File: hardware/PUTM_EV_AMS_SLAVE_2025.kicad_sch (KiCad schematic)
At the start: 7 parts, among them J1 TST-110-01-T-D, J2 M80-5100442, J4 M80-5100442

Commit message: pending
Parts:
- removed J2, J4: M80-5100442, Samacsys:M80-51004YY, symbol m80-5100442:M80-5100442
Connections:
- no-connect marks 4 -> 0

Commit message: layout done
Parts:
- removed C12, C5, C6, C9: 10nF/1kV, Capacitor_SMD:C_1206_3216Metric, symbol c2824c562jggacauto:C2824C562JGGACAUTO
- added C5, C6, C7, C8: 4.7nF/Y2, Samacsys:CAPC5728X280N, symbol Samacsys_kicad_sym:S252B222K502CT
- added J2, J3: B02B-PASK-1, Samacsys:B02BPASK1LFSN, symbol Samacsys_kicad_sym:B02B-PASK-1
- J1: footprint Connector_IDC:IDC-Header_2x09_P2.54mm_Vertical -> Connector_IDC:IDC-Header_2x10_P2.54mm_Vertical_SMD
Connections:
- net IN+: now also C7.1, J3.1 (Pin_1)
- net IN-: now also C8.1, J3.2 (Pin_2)
- net OUT+: now also C5.2, J2.1 (Pin_1)
- new net IA+: C7.2
- new net IA-: C8.2
- new net IB+: C5.1
- new net IB-: C6.1
- new net OUT-: C6.2, J2.2 (Pin_2)

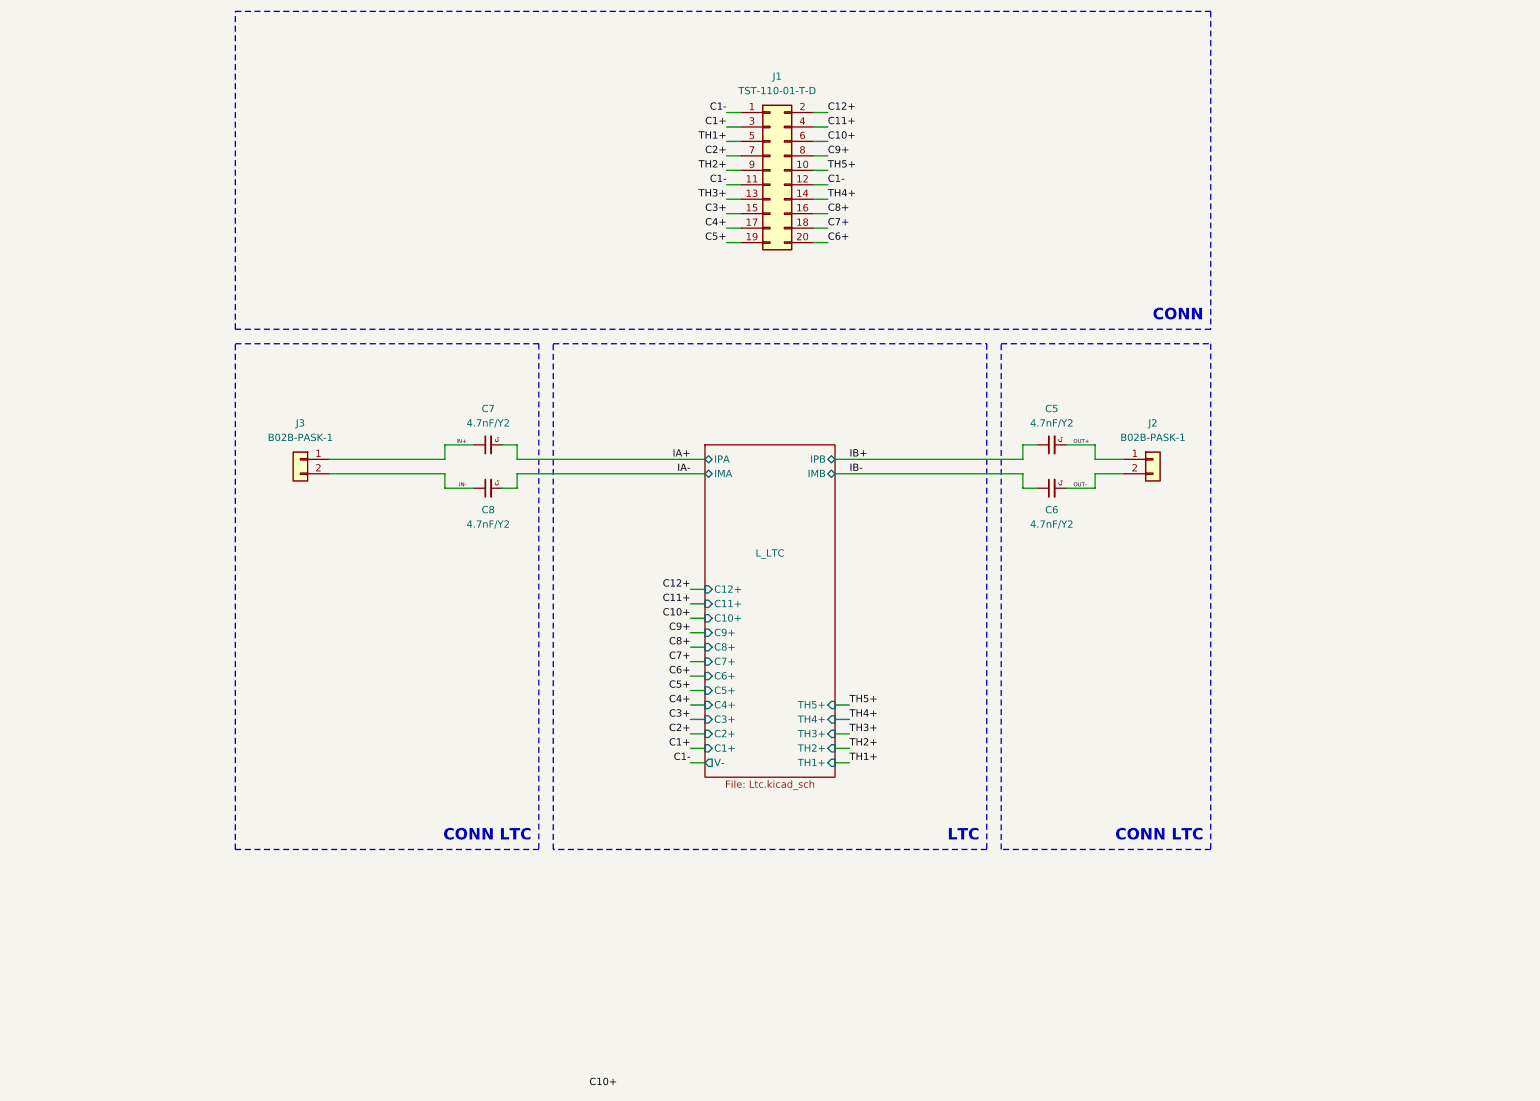
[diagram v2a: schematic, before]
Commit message: Bq ic balancing and measureing schematic part + main connector
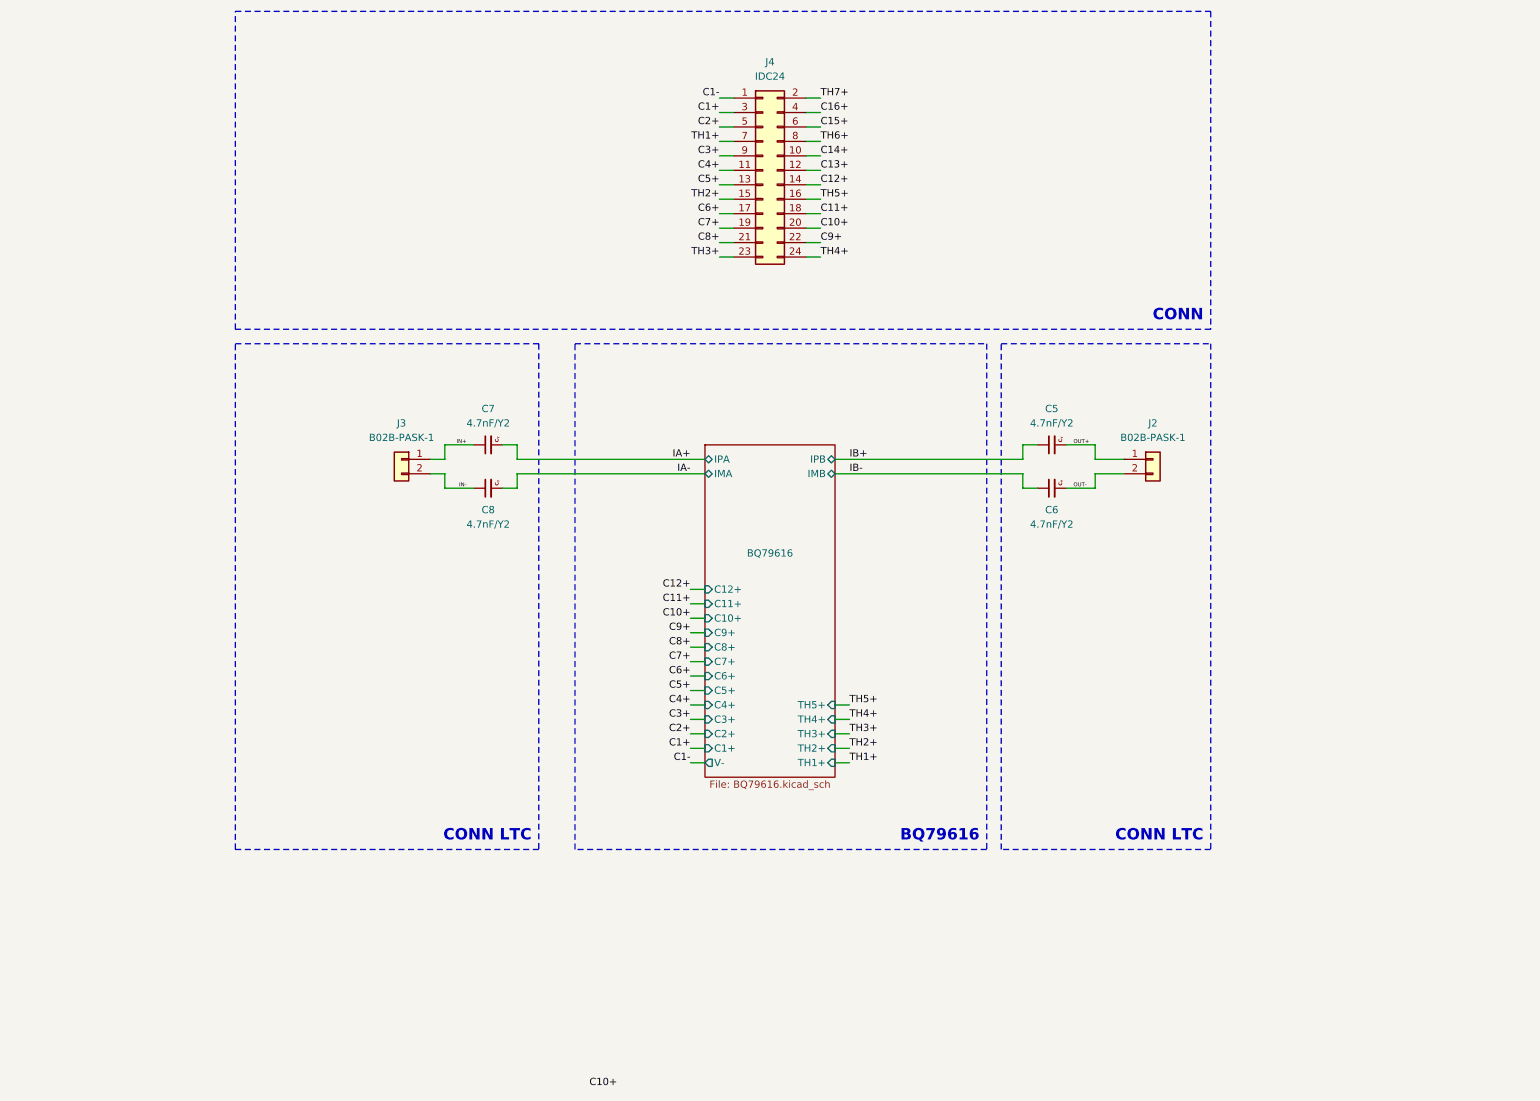
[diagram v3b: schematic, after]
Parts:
- removed J1: TST-110-01-T-D, Connector_IDC:IDC-Header_2x10_P2.54mm_Vertical_SMD, symbol Connector_Generic:Conn_02x10_Odd_Even
- added J4: IDC24, Connector_IDC:IDC-Header_2x12_P2.54mm_Vertical_SMD, symbol Connector_Generic:Conn_02x12_Odd_Even
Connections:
- net C1+: now also J4.3 (Pin_3)
- net C1-: now also J4.1 (Pin_1)
- net C10+: now also J4.20 (Pin_20)
- net C11+: now also J4.18 (Pin_18)
- net C12+: now also J4.14 (Pin_14)
- net C2+: now also J4.5 (Pin_5)
- net C3+: now also J4.9 (Pin_9)
- net C4+: now also J4.11 (Pin_11)
- net C5+: now also J4.13 (Pin_13)
- net C6+: now also J4.17 (Pin_17)
- net C7+: now also J4.19 (Pin_19)
- net C8+: now also J4.21 (Pin_21)
- net C9+: now also J4.22 (Pin_22)
- net TH1+: now also J4.7 (Pin_7)
- net TH2+: now also J4.15 (Pin_15)
- net TH3+: now also J4.23 (Pin_23)
- net TH4+: now also J4.24 (Pin_24)
- net TH5+: now also J4.16 (Pin_16)
- new net C13+: J4.12 (Pin_12)
- new net C14+: J4.10 (Pin_10)
- new net C15+: J4.6 (Pin_6)
- new net C16+: J4.4 (Pin_4)
- new net TH6+: J4.8 (Pin_8)
- new net TH7+: J4.2 (Pin_2)
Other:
- sheet L_LTC renamed BQ79616
- sheet BQ79616: file Ltc.kicad_sch -> BQ79616.kicad_sch
- note added: "BQ79616"
- note removed: "LTC"
- moved on the sheet: J3

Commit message: sync
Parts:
- added L1, L2: 100-500uH, Inductor_SMD:L_CommonModeChoke_Coilcraft_1812CAN, symbol Device:L_Coupled_Small_1243
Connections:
- net IN+: now also L1.2; no longer J3.1 (Pin_1)
- net IN-: now also L1.3; no longer J3.2 (Pin_2)
- net OUT+: now also L2.1; no longer J2.1 (Pin_1)
- net OUT-: now also L2.4; no longer J2.2 (Pin_2)
- new net: J2.1 (Pin_1), L2.2
- new net: J2.2 (Pin_2), L2.3
- new net: J3.1 (Pin_1), L1.1
- new net: J3.2 (Pin_2), L1.4
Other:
- sheet BQ79616 ports: added C13+, C14+, C15+, C16+, COMHN, COMHP, COMLN, COMLP; removed IMA, IMB, IPA, IPB
- moved on the sheet: C5, C6, C7, C8, J2, J3

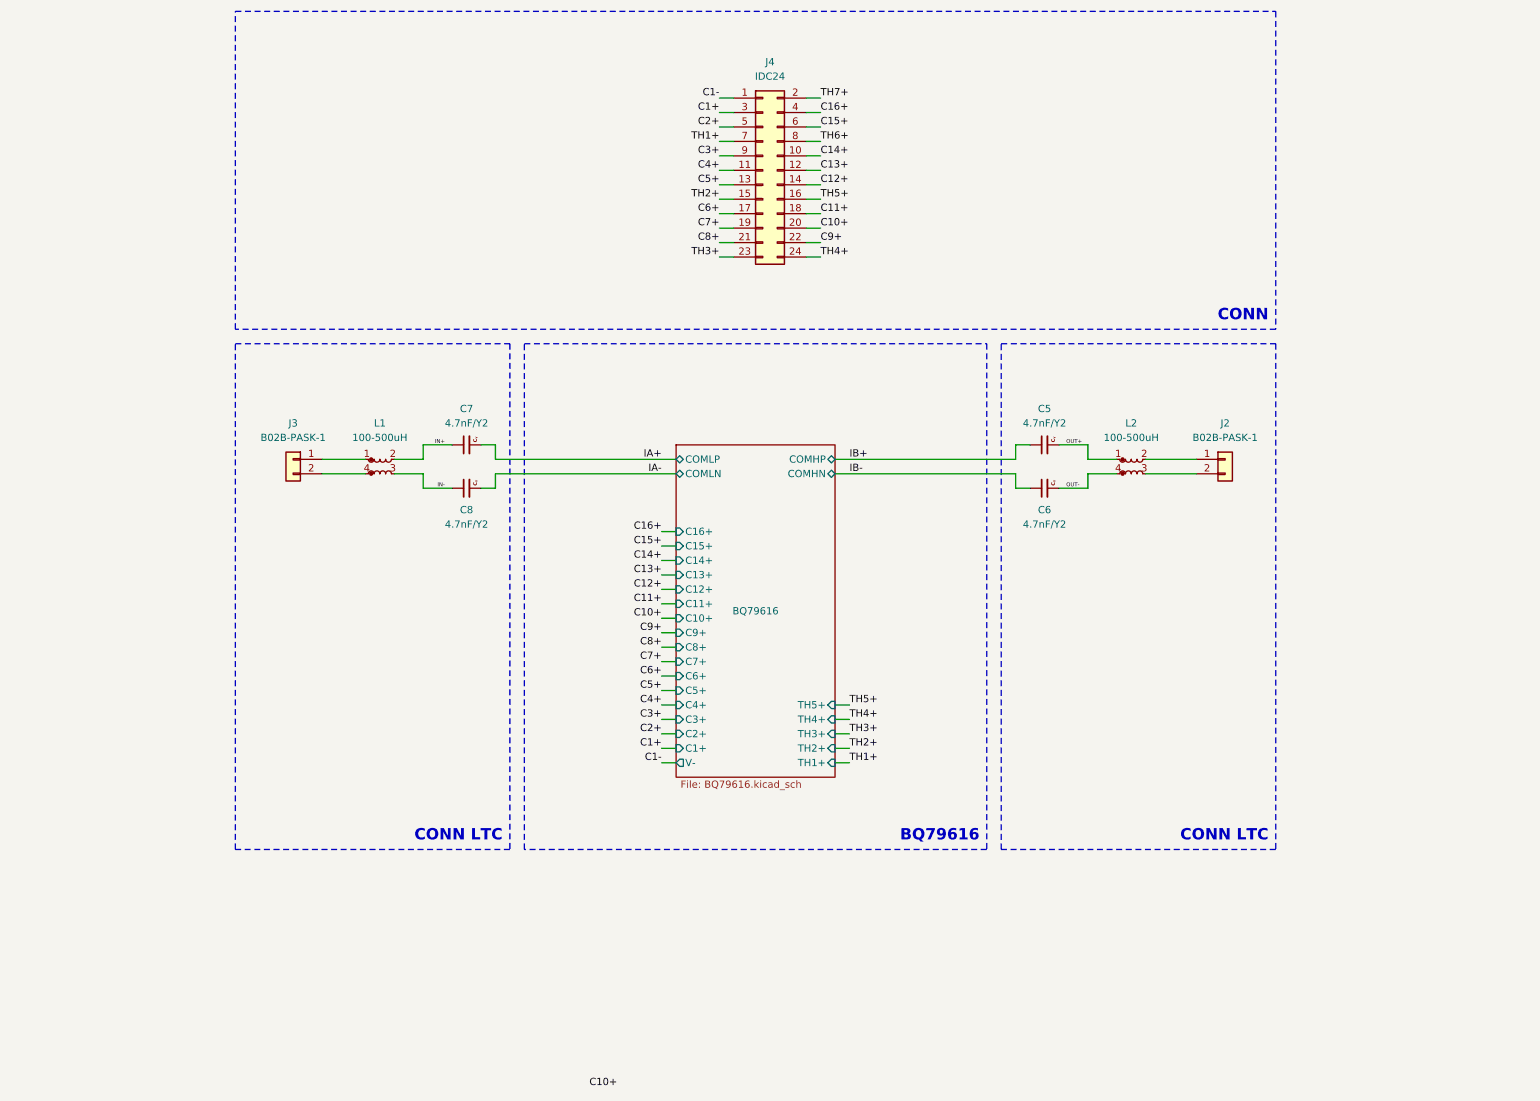
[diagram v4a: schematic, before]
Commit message: changed back harwin connectors, COM first fitting
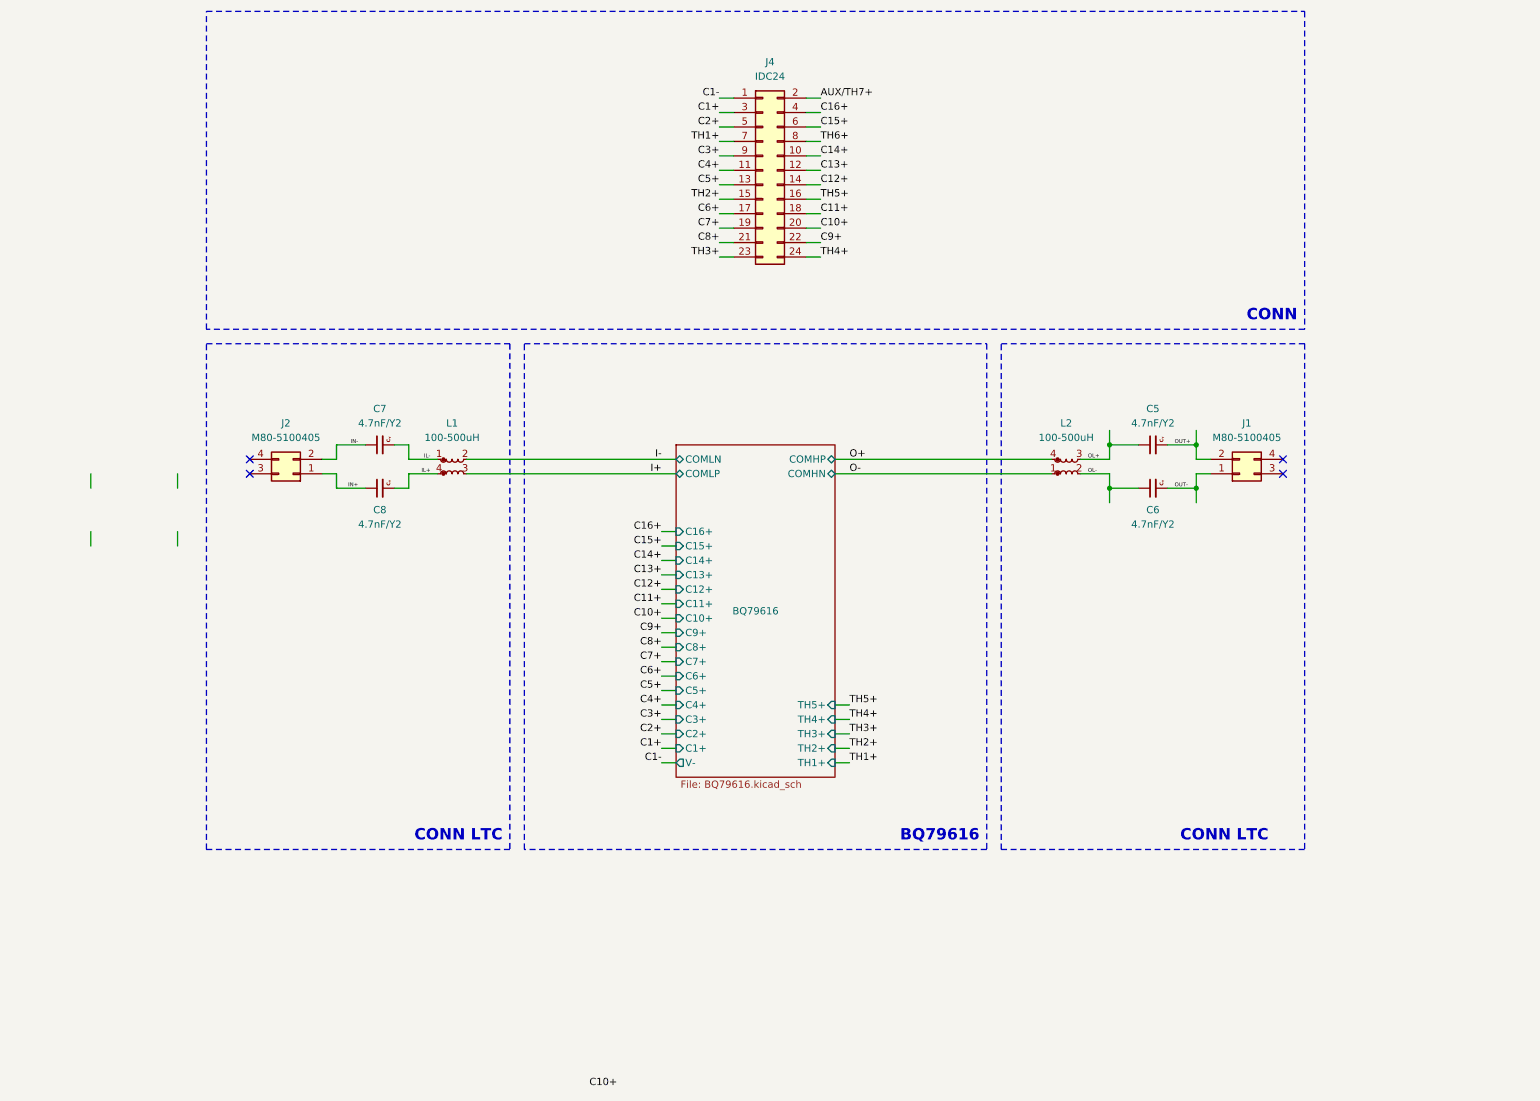
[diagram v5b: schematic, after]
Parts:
- removed J2, J3: B02B-PASK-1, Samacsys:B02BPASK1LFSN, symbol Samacsys_kicad_sym:B02B-PASK-1
- added J1, J2: M80-5100405, Samacsys:M80-51004YY, symbol Samacsys_kicad_sym:M80-5100405
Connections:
- net IA+ is gone; now on net IL-: C7.2
- net IA- is gone; now on net IL+: C8.2
- net IB+ is gone; now on net OL+: C5.1
- net IB- is gone; now on net OL-: C6.1
- net IN+: now also C8.1, J2.1 (Pin_1); no longer C7.1, L1.2
- net IN-: now also C7.1, J2.2 (Pin_2); no longer C8.1, L1.3
- net OUT+: now also J1.2 (Pin_2); no longer L2.1
- net OUT-: now also J1.1 (Pin_1); no longer L2.4
- net OL-: now reaches L2.2
- net OL+: now reaches L2.3
- net IL-: now reaches L1.1
- net IL+: now reaches L1.4
- net TH7+ renamed AUX/TH7+
- new net I+: L1.3
- new net I-: L1.2
- new net O+: L2.4
- new net O-: L2.1
- no-connect marks 0 -> 4
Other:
- moved on the sheet: C5, C6, C7, C8, L1, L2

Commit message: sync
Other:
- moved on the sheet: C5, C6, C7, C8, J1, J2, L1, L2
